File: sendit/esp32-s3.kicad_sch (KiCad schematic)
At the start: 45 parts, among them J9 USB_TYPE_C_16PIN, Q1 FDC6330L, Q2 S8050, Q3 S8050, SW1 RESET, SW2 BOOT, U1 ESP32-S3-WROOM-1-N16R8, U2 USBLC6-2SC6, U3 XC6210B332MR, U4 CH334F, U5 CH343P, Y1 12Mhz, Y2 32.768kHz

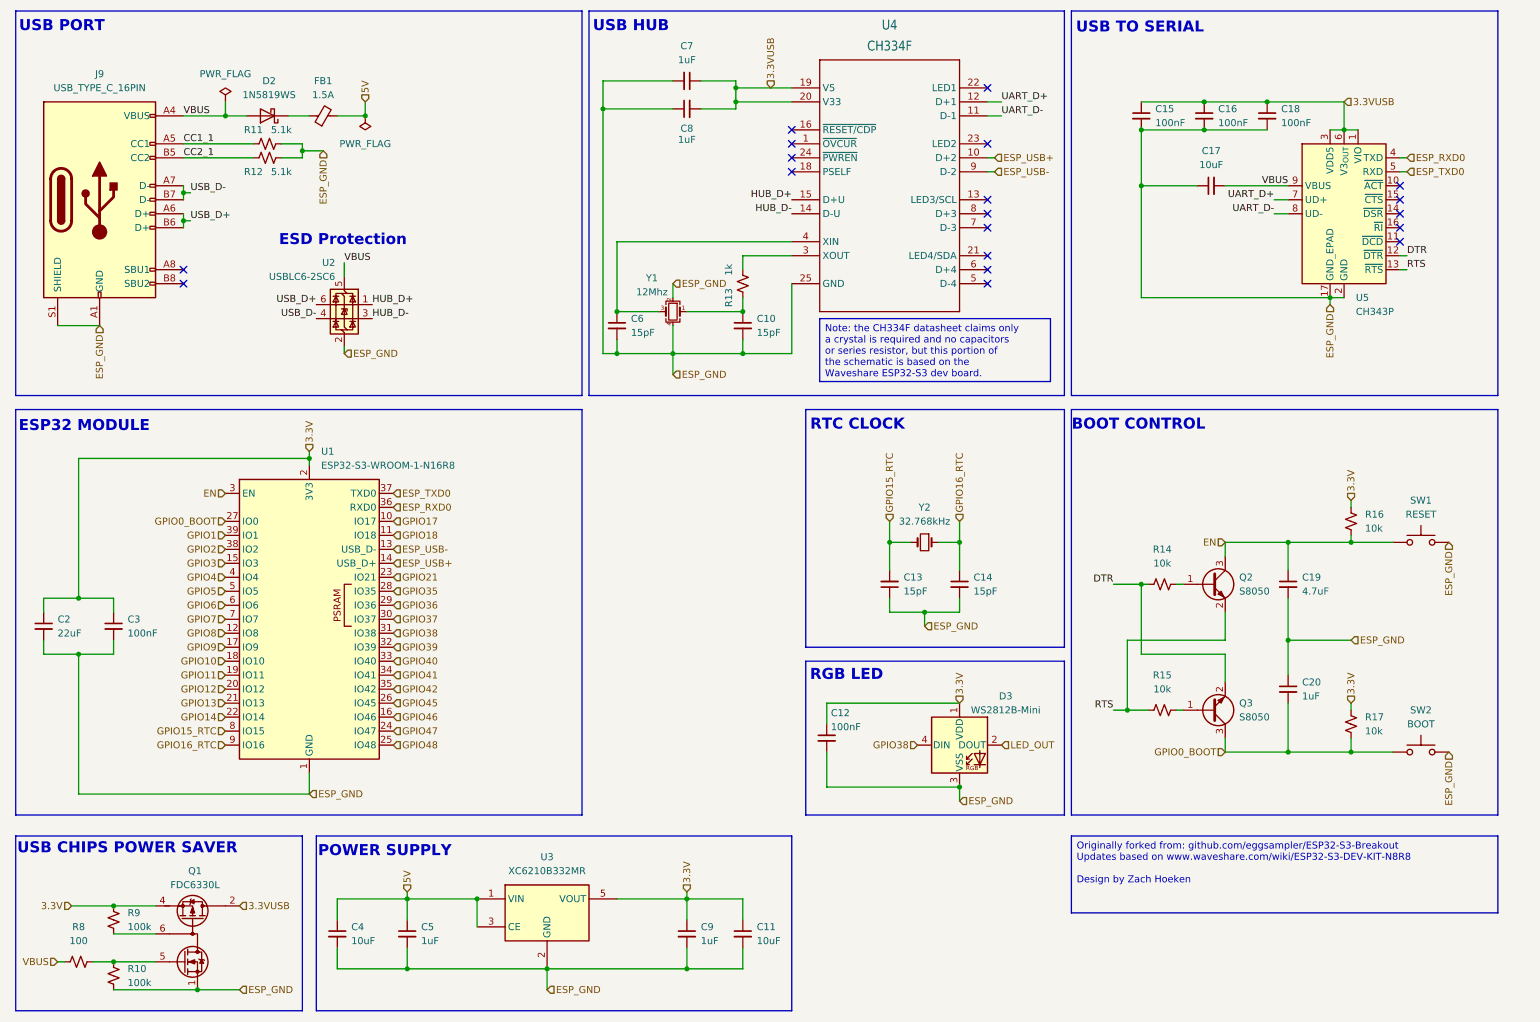
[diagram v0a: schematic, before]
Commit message: brought over the latest esp32-s3 schematic
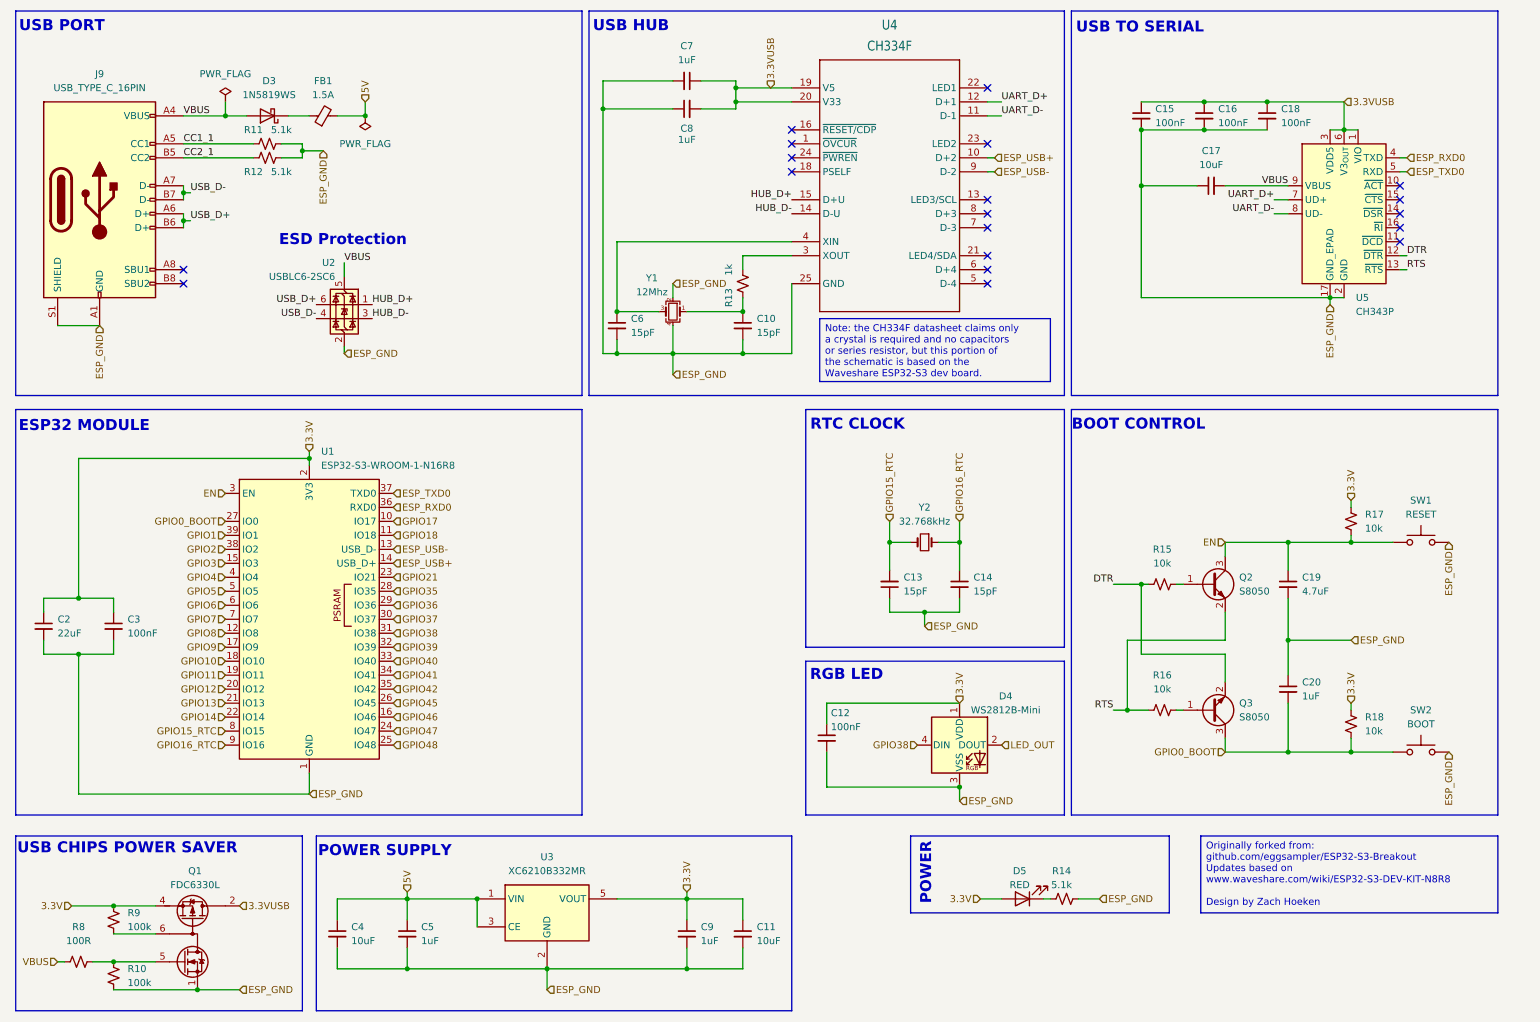
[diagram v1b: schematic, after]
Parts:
- added D5: RED, LED_SMD:LED_0603_1608Metric, symbol Device:LED
- added R14: 5.1k, Resistor_SMD:R_0603_1608Metric, symbol Device:R_Small_US
- D3: renamed from D2; LCSC (none) -> C191023
- J9: Position Offset (none) -> 0.0,1.27
- Q1: LCSC (none) -> C112086
- R8: value 100 -> 100R
- SW1, SW2: LCSC C843684 -> C557599; Rotation Offset (none) -> 180
- U1: LCSC (none) -> C2913202; Position Offset (none) -> 0,-3.6195
- U2: Rotation Offset (none) -> 90
- U3: LCSC (none) -> C424705
- U4: LCSC (none) -> C5187527; Rotation Offset (none) -> 180
- U5: LCSC (none) -> C2846043; Rotation Offset (none) -> 180
- renumbered D3 to D4, R14 to R15, R15 to R16, R16 to R17, R17 to R18
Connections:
- net 3.3V: now also D5.2 (A)
- net ESP_GND: now also R14.2
- new net: D5.1 (K), R14.1
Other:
- note added: "POWER"

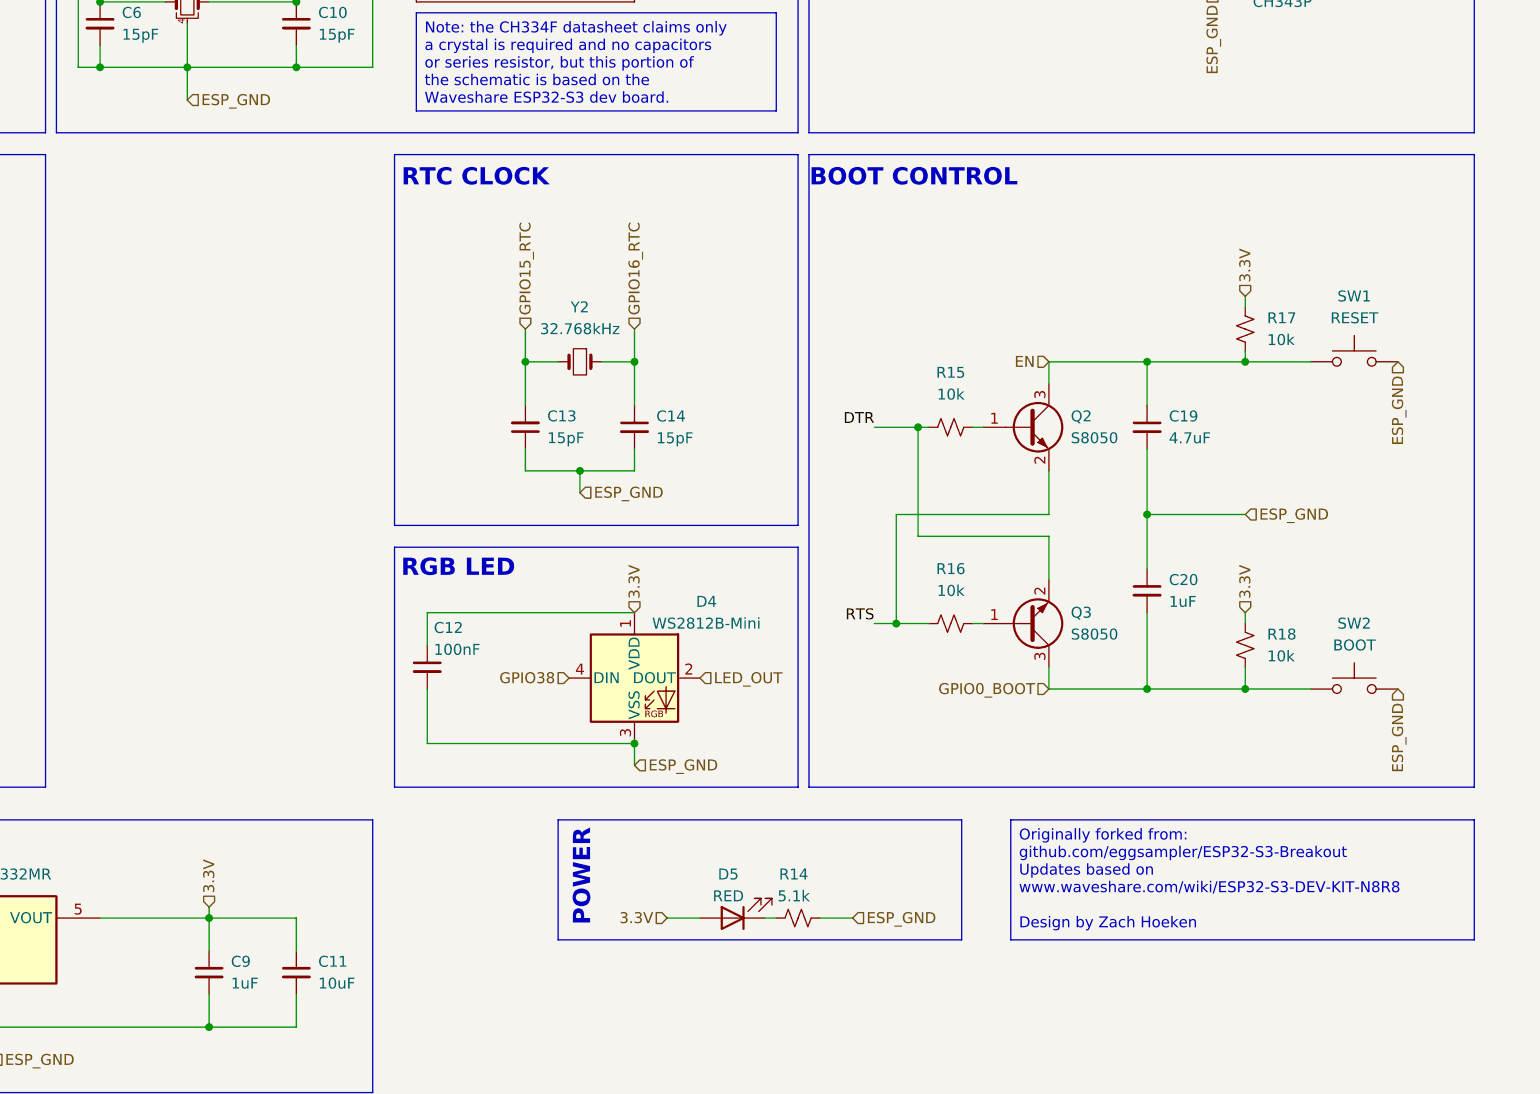
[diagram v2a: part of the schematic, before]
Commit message: cleaning up schematics a bit for design review
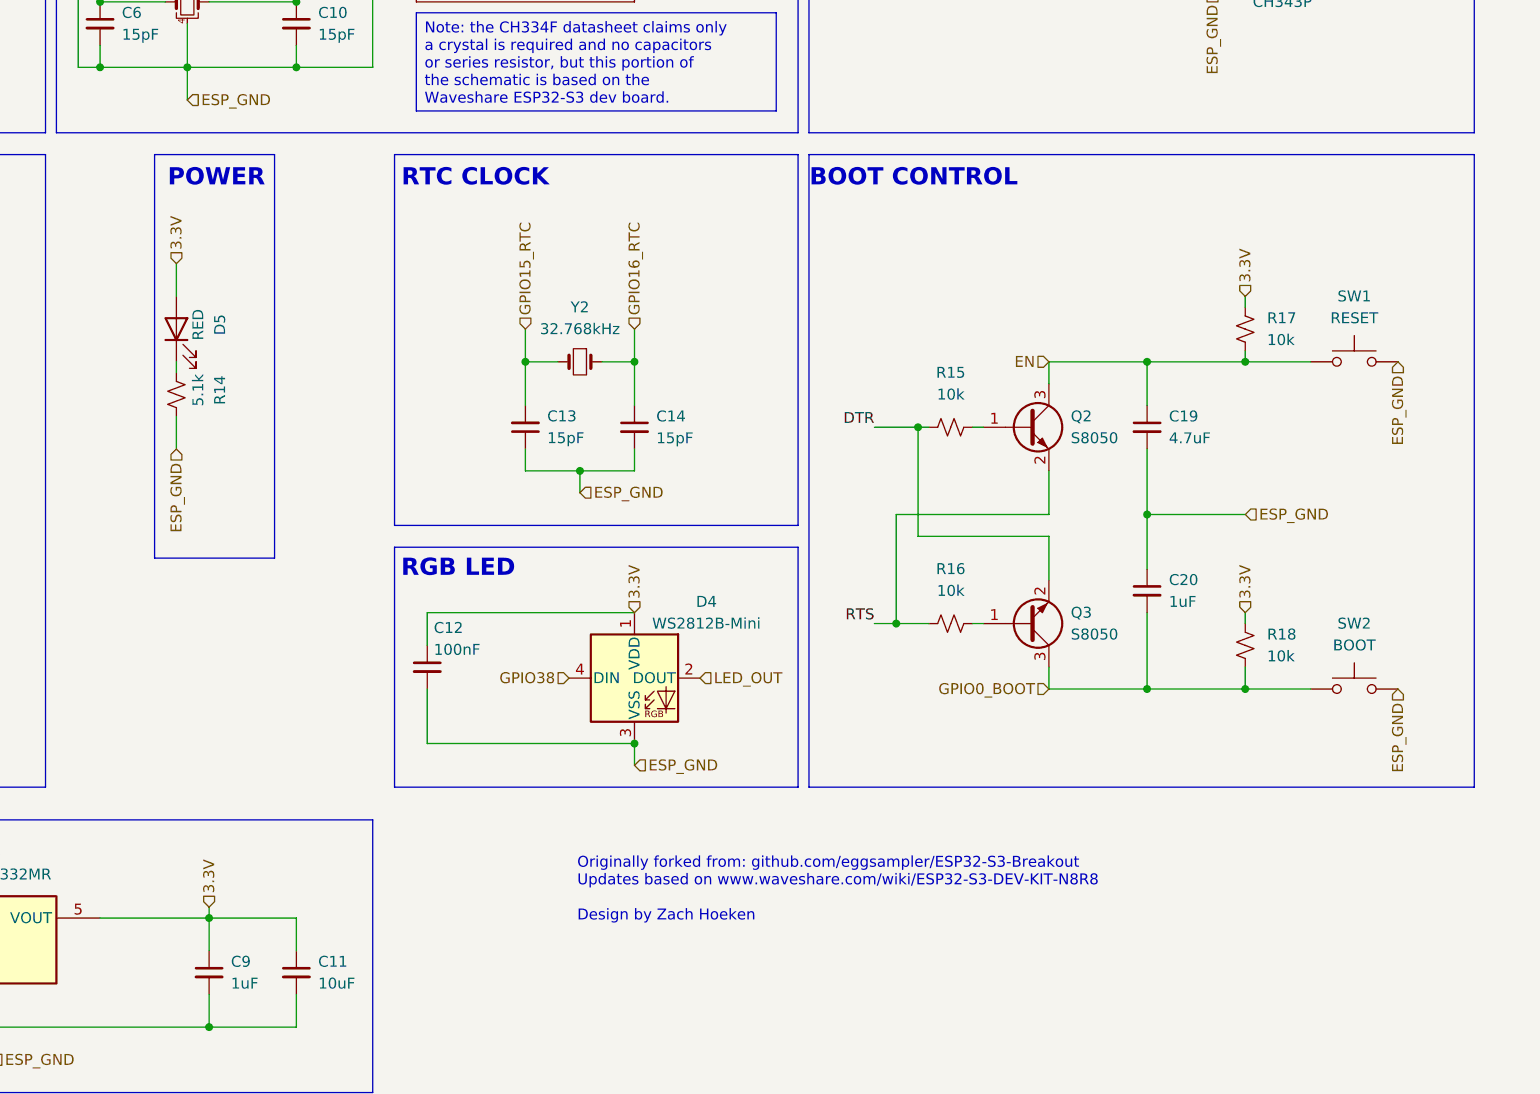
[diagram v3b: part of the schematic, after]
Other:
- title: https://github.com/hoeken/ESP32-S3-Template -> https://github.com/hoeken/sendit
- moved on the sheet: D5, R14
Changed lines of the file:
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@@
 	(paper "A4")
 	(title_block
-		(title "https://github.com/hoeken/ESP32-S3-Template")
+		(title "https://github.com/hoeken/sendit")
 		(date "2025-08-28")
-		(rev "A")
+		(rev "B")
 	)
 	(rectangle
@@
 	)
 	(rectangle
-		(start 176.53 163.83)
-		(end 223.52 177.8)
+		(start 143.51 86.36)
+		(end 129.54 133.35)
 		(stroke
 			(width 0)
@@
 	(text "POWER"
 		(exclude_from_sim no)
-		(at 179.324 176.276 90)
+		(at 131.064 89.154 0)
 		(effects
 			(font
@@
 	(text_box "Originally forked from: github.com/eggsampler/ESP32-S3-Breakout\nUpdates based on www.waveshare.com/wiki/ESP32-S3-DEV-KIT-N8R8\n\nDesign by Zach Hoeken"
 		(exclude_from_sim no)
-		(at 229.235 163.83 0)
-		(size 53.975 13.97)
+		(at 177.8 167.005 0)
+		(size 105.41 13.97)
 		(margins 0.9525 0.9525 0.9525 0.9525)
 		(stroke
-			(width 0)
+			(width -0.0001)
 			(type solid)
 		)
@@
 	(wire
 		(pts
-			(xy 189.23 175.26) (xy 193.04 175.26)
+			(xy 132.08 99.06) (xy 132.08 102.87)
 		)
 		(stroke
@@
 	(wire
 		(pts
-			(xy 200.66 175.26) (xy 201.93 175.26)
+			(xy 132.08 110.49) (xy 132.08 111.76)
 		)
 		(stroke
@@
 	(wire
 		(pts
-			(xy 207.01 175.26) (xy 210.82 175.26)
+			(xy 132.08 116.84) (xy 132.08 120.65)
 		)
 		(stroke
@@
 	(hierarchical_label "ESP_GND"
 		(shape input)
-		(at 210.82 175.26 0)
+		(at 132.08 120.65 270)
 		(effects
 			(font
 				(size 1.27 1.27)
 			)
-			(justify left)
+			(justify right)
 		)
 	)
@@
 	(hierarchical_label "3.3V"
 		(shape input)
-		(at 189.23 175.26 180)
+		(at 132.08 99.06 90)
 		(effects
 			(font
 				(size 1.27 1.27)
 			)
-			(justify right)
+			(justify left)
 		)
 	)
@@
 	(symbol
 		(lib_id "Device:LED")
-		(at 196.85 175.26 180)
+		(at 132.08 106.68 90)
 		(unit 1)
 		(exclude_from_sim no)
@@
 		(dnp no)
 		(property "Reference" "D5"
-			(at 196.342 170.18 0)
+			(at 137.16 106.172 0)
 			(effects
 				(font
@@
 		)
 		(property "Value" "RED"
-			(at 196.342 172.72 0)
+			(at 134.62 106.172 0)
 			(effects
 				(font
@@
 		)
 		(property "Footprint" "LED_SMD:LED_0603_1608Metric"
-			(at 196.85 175.26 0)
+			(at 132.08 106.68 0)
 			(effects
 				(font
@@
 		)
 		(property "Datasheet" "~"
-			(at 196.85 175.26 0)
+			(at 132.08 106.68 0)
 			(effects
 				(font
@@
 		)
 		(property "Description" "Light emitting diode"
-			(at 196.85 175.26 0)
+			(at 132.08 106.68 0)
 			(effects
 				(font
@@
 		)
 		(property "Sim.Pins" "1=K 2=A"
-			(at 196.85 175.26 0)
+			(at 132.08 106.68 0)
 			(effects
 				(font
@@
 		)
 		(property "LCSC" "C965799"
-			(at 196.85 175.26 0)
+			(at 132.08 106.68 0)
 			(effects
 				(font
@@
 		)
 		(property "LCSC Part Name" ""
-			(at 196.85 175.26 0)
+			(at 132.08 106.68 0)
 			(effects
 				(font
@@
 		)
 		(property "Manufacturer" ""
-			(at 196.85 175.26 0)
+			(at 132.08 106.68 0)
 			(effects
 				(font
@@
 		)
 		(property "Manufacturer Part" ""
-			(at 196.85 175.26 0)
+			(at 132.08 106.68 0)
 			(effects
 				(font
@@
 		)
 		(property "Supplier" ""
-			(at 196.85 175.26 0)
+			(at 132.08 106.68 0)
 			(effects
 				(font
@@
 		)
 		(property "Supplier Part" ""
-			(at 196.85 175.26 0)
+			(at 132.08 106.68 0)
 			(effects
 				(font
@@
 	(symbol
 		(lib_id "Device:R_Small_US")
-		(at 204.47 175.26 90)
+		(at 132.08 114.3 0)
 		(unit 1)
 		(exclude_from_sim no)
@@
 		(dnp no)
 		(property "Reference" "R14"
-			(at 203.962 170.18 90)
+			(at 137.16 113.792 90)
 			(effects
 				(font
@@
 		)
 		(property "Value" "5.1k"
-			(at 203.962 172.72 90)
+			(at 134.62 113.792 90)
 			(effects
 				(font
@@
 		)
 		(property "Footprint" "Resistor_SMD:R_0603_1608Metric"
-			(at 204.47 175.26 0)
+			(at 132.08 114.3 0)
 			(effects
 				(font
@@
 		)
 		(property "Datasheet" "~"
-			(at 204.47 175.26 0)
+			(at 132.08 114.3 0)
 			(effects
 				(font
@@
 		)
 		(property "Description" "Resistor, small US symbol"
-			(at 204.47 175.26 0)
+			(at 132.08 114.3 0)
 			(effects
 				(font
@@
 		)
 		(property "LCSC Part Name" ""
-			(at 204.47 175.26 90)
+			(at 132.08 114.3 90)
 			(effects
 				(font
@@
 		)
 		(property "Manufacturer" ""
-			(at 204.47 175.26 90)
+			(at 132.08 114.3 90)
 			(effects
 				(font
@@
 		)
 		(property "Manufacturer Part" ""
-			(at 204.47 175.26 90)
+			(at 132.08 114.3 90)
 			(effects
 				(font
@@
 		)
 		(property "Supplier" ""
-			(at 204.47 175.26 90)
+			(at 132.08 114.3 90)
 			(effects
 				(font
@@
 		)
 		(property "Supplier Part" ""
-			(at 204.47 175.26 90)
+			(at 132.08 114.3 90)
 			(effects
 				(font
